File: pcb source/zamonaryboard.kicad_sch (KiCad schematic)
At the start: 17 parts, among them J1 USB_C_Receptacle_USB2.0_14P, SW1 SW_Push, U1 ESP32-S2, U2 ME6211C33M5, Y1 Crystal_GND24

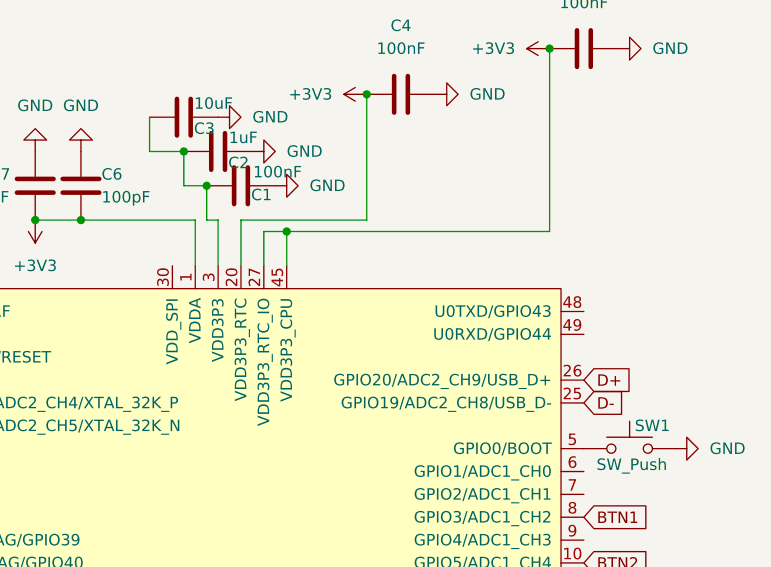
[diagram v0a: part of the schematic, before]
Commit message: Added jlcpcb component annotations, small improvements
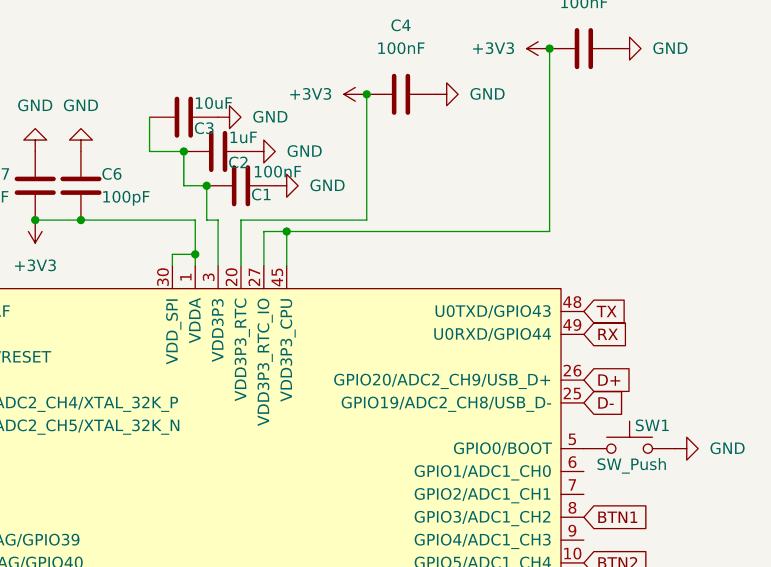
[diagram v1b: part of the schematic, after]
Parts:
- C1, C4, C5: LCSC (none) -> C14663
- C2, C7: LCSC (none) -> C15849
- C3: LCSC (none) -> C19702
- C6: LCSC (none) -> C14665
- C8, C9: LCSC (none) -> C63339
- R1, R2: LCSC (none) -> C23186
- Y1: LCSC (none) -> C9010
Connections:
- net +3V3: now also U1.30 (VDD_SPI)
- net TX: now reaches U1.48 (U0TXD/GPIO43)
- net RX: now reaches U1.49 (U0RXD/GPIO44)
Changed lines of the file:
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@@
 	)
 	(junction
+		(at 134.62 48.26)
+		(diameter 0)
+		(color 0 0 0 0)
+	)
+	(junction
 		(at 39.37 114.3)
 		(diameter 0)
@@
 	(wire
 		(pts
+			(xy 137.16 44.45) (xy 137.16 49.53)
+		)
+		(stroke
+			(width 0)
+			(type default)
+		)
+	)
+	(wire
+		(pts
 			(xy 133.35 36.83) (xy 133.35 40.64)
 		)
@@
 	(wire
 		(pts
-			(xy 137.16 49.53) (xy 137.16 44.45)
+			(xy 50.8 48.26) (xy 53.34 48.26)
 		)
 		(stroke
@@
 	(wire
 		(pts
-			(xy 50.8 48.26) (xy 53.34 48.26)
+			(xy 95.25 74.93) (xy 95.25 77.47)
 		)
 		(stroke
@@
 	(wire
 		(pts
-			(xy 95.25 74.93) (xy 95.25 77.47)
+			(xy 53.34 43.18) (xy 53.34 40.64)
 		)
 		(stroke
@@
 	(wire
 		(pts
-			(xy 53.34 43.18) (xy 53.34 40.64)
+			(xy 95.25 69.85) (xy 95.25 72.39)
 		)
 		(stroke
@@
 	(wire
 		(pts
-			(xy 95.25 69.85) (xy 95.25 72.39)
+			(xy 134.62 48.26) (xy 134.62 44.45)
 		)
 		(stroke
@@
 	(wire
 		(pts
+			(xy 132.08 48.26) (xy 134.62 48.26)
+		)
+		(stroke
+			(width 0)
+			(type default)
+		)
+	)
+	(wire
+		(pts
 			(xy 95.25 72.39) (xy 101.6 72.39)
 		)
@@
 	(wire
 		(pts
-			(xy 134.62 49.53) (xy 134.62 44.45)
+			(xy 134.62 49.53) (xy 134.62 48.26)
 		)
 		(stroke
@@
 	(wire
 		(pts
+			(xy 132.08 48.26) (xy 132.08 49.53)
+		)
+		(stroke
+			(width 0)
+			(type default)
+		)
+	)
+	(wire
+		(pts
 			(xy 153.67 44.45) (xy 153.67 30.48)
 		)
@@
 		)
 	)
+	(global_label "TX"
+		(shape input)
+		(at 177.8 54.61 0)
+		(fields_autoplaced yes)
+		(effects
+			(font
+				(size 1.27 1.27)
+			)
+			(justify left)
+		)
+		(property "Intersheetrefs" "${INTERSHEET_REFS}"
+			(at 182.9623 54.61 0)
+			(effects
+				(font
+					(size 1.27 1.27)
+				)
+				(justify left)
+				(hide yes)
+			)
+		)
+	)
 	(global_label "D+"
 		(shape input)
@@
 		)
 	)
+	(global_label "RX"
+		(shape input)
+		(at 177.8 57.15 0)
+		(fields_autoplaced yes)
+		(effects
+			(font
+				(size 1.27 1.27)
+			)
+			(justify left)
+		)
+		(property "Intersheetrefs" "${INTERSHEET_REFS}"
+			(at 183.2647 57.15 0)
+			(effects
+				(font
+					(size 1.27 1.27)
+				)
+				(justify left)
+				(hide yes)
+			)
+		)
+	)
 	(global_label "D-"
 		(shape input)
@@
 			)
 		)
+		(property "LCSC" "C14665"
+			(at 121.92 40.64 0)
+			(effects
+				(font
+					(size 1.27 1.27)
+				)
+				(hide yes)
+			)
+		)
 		(pin "2"
 		)
@@
 			)
 		)
+		(property "LCSC" "C19702"
+			(at 133.35 33.02 90)
+			(effects
+				(font
+					(size 1.27 1.27)
+				)
+				(hide yes)
+			)
+		)
 		(pin "2"
 		)
@@
 			)
 		)
+		(property "LCSC" "C9010"
+			(at 71.12 73.66 90)
+			(effects
+				(font
+					(size 1.27 1.27)
+				)
+				(hide yes)
+			)
+		)
 		(pin "3"
 		)
@@
 			)
 		)
+		(property "LCSC" "C14663"
+			(at 177.8 25.4 90)
+			(effects
+				(font
+					(size 1.27 1.27)
+				)
+				(hide yes)
+			)
+		)
 		(pin "2"
 		)
@@
 			)
 		)
+		(property "LCSC" "C15849"
+			(at 137.16 36.83 90)
+			(effects
+				(font
+					(size 1.27 1.27)
+				)
+				(hide yes)
+			)
+		)
 		(pin "2"
 		)
@@
 			)
 		)
+		(property "LCSC" "C14663"
+			(at 139.7 40.64 90)
+			(effects
+				(font
+					(size 1.27 1.27)
+				)
+				(hide yes)
+			)
+		)
 		(pin "2"
 		)
@@
 			)
 		)
+		(property "LCSC" "C15849"
+			(at 116.84 40.64 0)
+			(effects
+				(font
+					(size 1.27 1.27)
+				)
+				(hide yes)
+			)
+		)
 		(pin "2"
 		)
@@
 			)
 		)
+		(property "LCSC" "C63339"
+			(at 63.5 83.82 90)
+			(effects
+				(font
+					(size 1.27 1.27)
+				)
+				(hide yes)
+			)
+		)
 		(pin "2"
 		)
@@
 			)
 		)
+		(property "LCSC" "C14663"
+			(at 157.48 30.48 90)
+			(effects
+				(font
+					(size 1.27 1.27)
+				)
+				(hide yes)
+			)
+		)
 		(pin "2"
 		)
@@
 			)
 		)
+		(property "LCSC" "C63339"
+			(at 63.5 63.5 90)
+			(effects
+				(font
+					(size 1.27 1.27)
+				)
+				(hide yes)
+			)
+		)
 		(pin "2"
 		)
@@
 			)
 		)
+		(property "LCSC" "C23186"
+			(at 54.61 33.02 90)
+			(effects
+				(font
+					(size 1.27 1.27)
+				)
+				(hide yes)
+			)
+		)
 		(pin "2"
 		)
@@
 			(effects
 				(font
+					(size 1.27 1.27)
+				)
+				(hide yes)
+			)
+		)
+		(property "LCSC" "C23186"
+			(at 54.61 35.56 90)
+			(effects
+				(font

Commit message: big improvements to pcb
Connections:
- net +3V3: now also C1.1, C2.1, C3.1, U1.3 (VDD3P3), U1.4 (VDD3P3)
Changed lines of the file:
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@@
+	)
+	(junction
+		(at 129.54 33.02)
+		(diameter 0)
+		(color 0 0 0 0)
 	)
 	(junction
@@
 					(unit 1)
 				)
+			)
+		)
+	)
+	(symbol
+		(lib_id "power:+3V3")
+		(at 129.54 33.02 0)
+		(unit 1)
+		(exclude_from_sim no)
+		(in_bom yes)
+		(on_board yes)
+		(dnp no)
+		(property "Reference" "#PWR026"
+			(at 129.54 36.83 0)
+			(effects
+				(font
+					(size 1.27 1.27)
+				)
+				(hide yes)
+			)
+		)
+		(property "Value" "+3V3"
+			(at 128.524 29.718 0)
+			(effects
+				(font
+					(size 1.27 1.27)
+				)
+			)
+		)
+		(property "Footprint" ""
+			(at 129.54 33.02 0)
+			(effects
+				(font
+					(size 1.27 1.27)
+				)
+				(hide yes)
+			)
+		)
+		(property "Datasheet" ""
+			(at 129.54 33.02 0)
+			(effects
+				(font
+					(size 1.27 1.27)
+				)
+				(hide yes)
+			)
+		)
+		(property "Description" "Power symbol creates a global label with name \"+3V3\""
+			(at 129.54 33.02 0)
+			(effects
+				(font
+					(size 1.27 1.27)
+				)
+				(hide yes)
+			)
+		)
+		(pin "1"
+		)
+		(instances
+			(project "zamonaryboard"
+				(path "/d5ea9308-ab10-4197-867c-fba653905f7c"
+					(reference "#PWR026")
+					(unit 1)
+				)

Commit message: exported gerber files for prototype 1.3, cleanup
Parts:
- C8, C9: footprint Capacitor_SMD:C_0805_2012Metric_Pad1.18x1.45mm_HandSolder -> Capacitor_SMD:C_0603_1608Metric_Pad1.08x0.95mm_HandSolder
- Y1: footprint Crystal:Crystal_SMD_3225-4Pin_3.2x2.5mm_HandSoldering -> Crystal:Crystal_SMD_3225-4Pin_3.2x2.5mm
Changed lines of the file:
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@@
 			)
 		)
-		(property "Footprint" "Crystal:Crystal_SMD_3225-4Pin_3.2x2.5mm_HandSoldering"
+		(property "Footprint" "Crystal:Crystal_SMD_3225-4Pin_3.2x2.5mm"
 			(at 71.12 73.66 0)
 			(effects
@@
 			)
 		)
-		(property "Footprint" "Capacitor_SMD:C_0805_2012Metric_Pad1.18x1.45mm_HandSolder"
+		(property "Footprint" "Capacitor_SMD:C_0603_1608Metric_Pad1.08x0.95mm_HandSolder"
 			(at 67.31 82.8548 0)
 			(effects
@@
 			)
 		)
-		(property "Footprint" "Capacitor_SMD:C_0805_2012Metric_Pad1.18x1.45mm_HandSolder"
+		(property "Footprint" "Capacitor_SMD:C_0603_1608Metric_Pad1.08x0.95mm_HandSolder"
 			(at 67.31 62.5348 0)
 			(effects

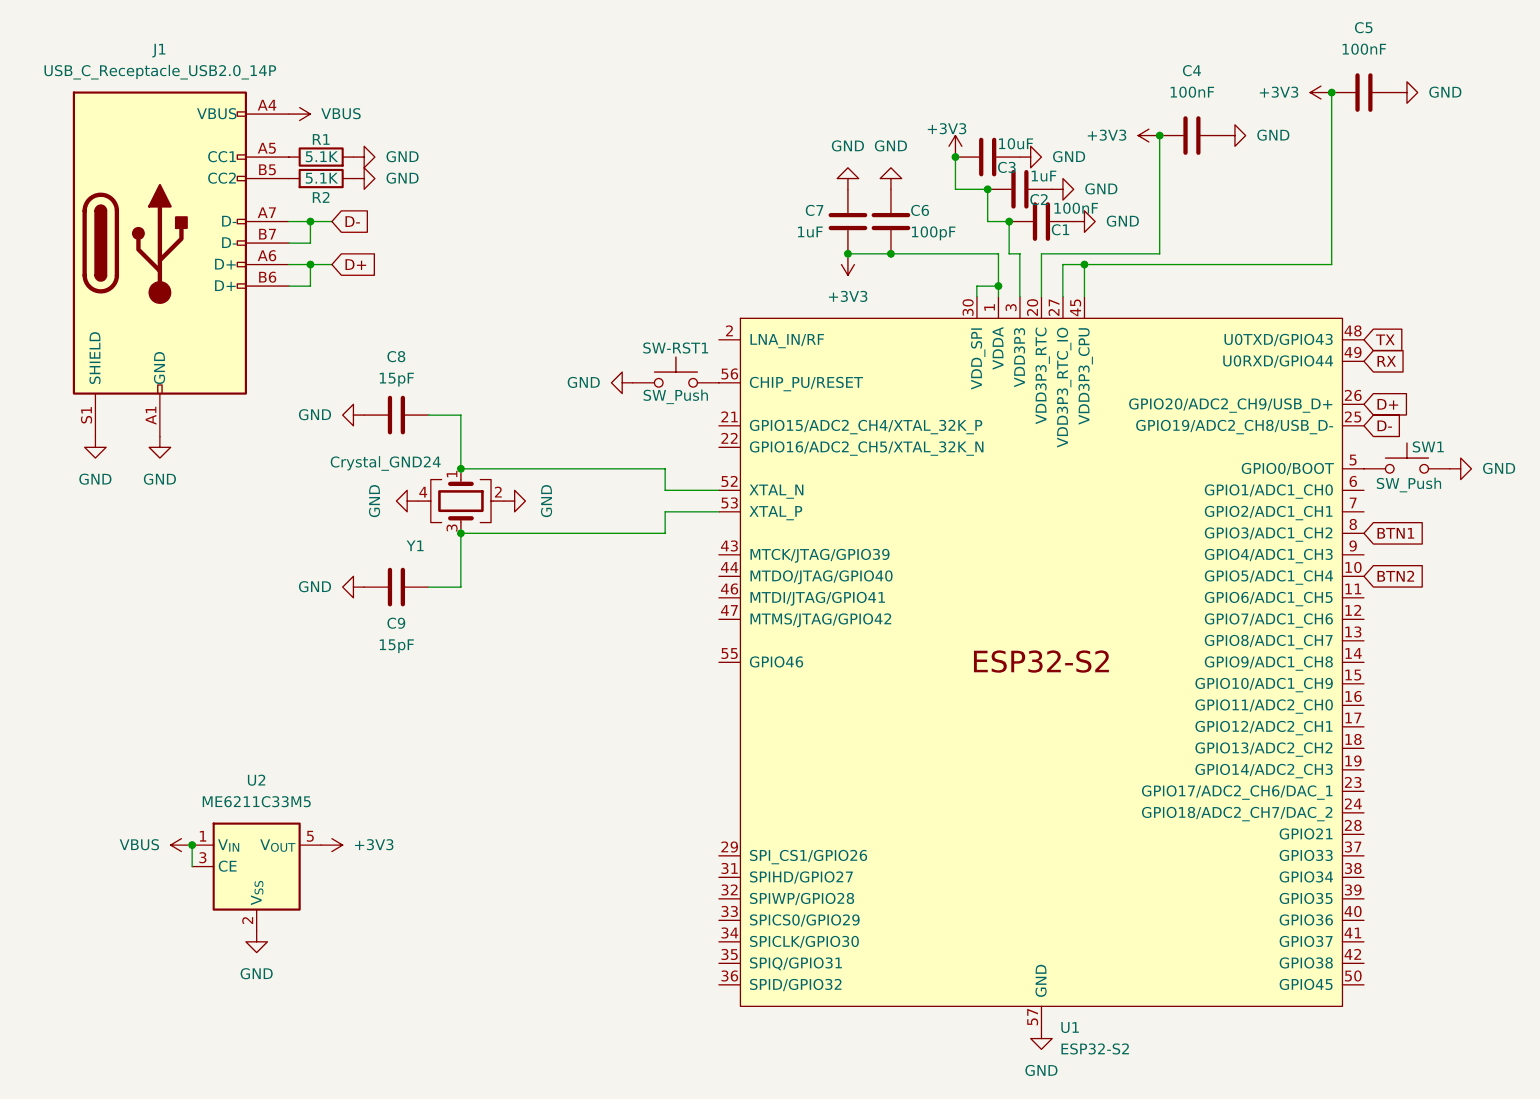
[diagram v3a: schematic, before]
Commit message: Many improvements to pcb and scheme, added testpoints for easier debugging
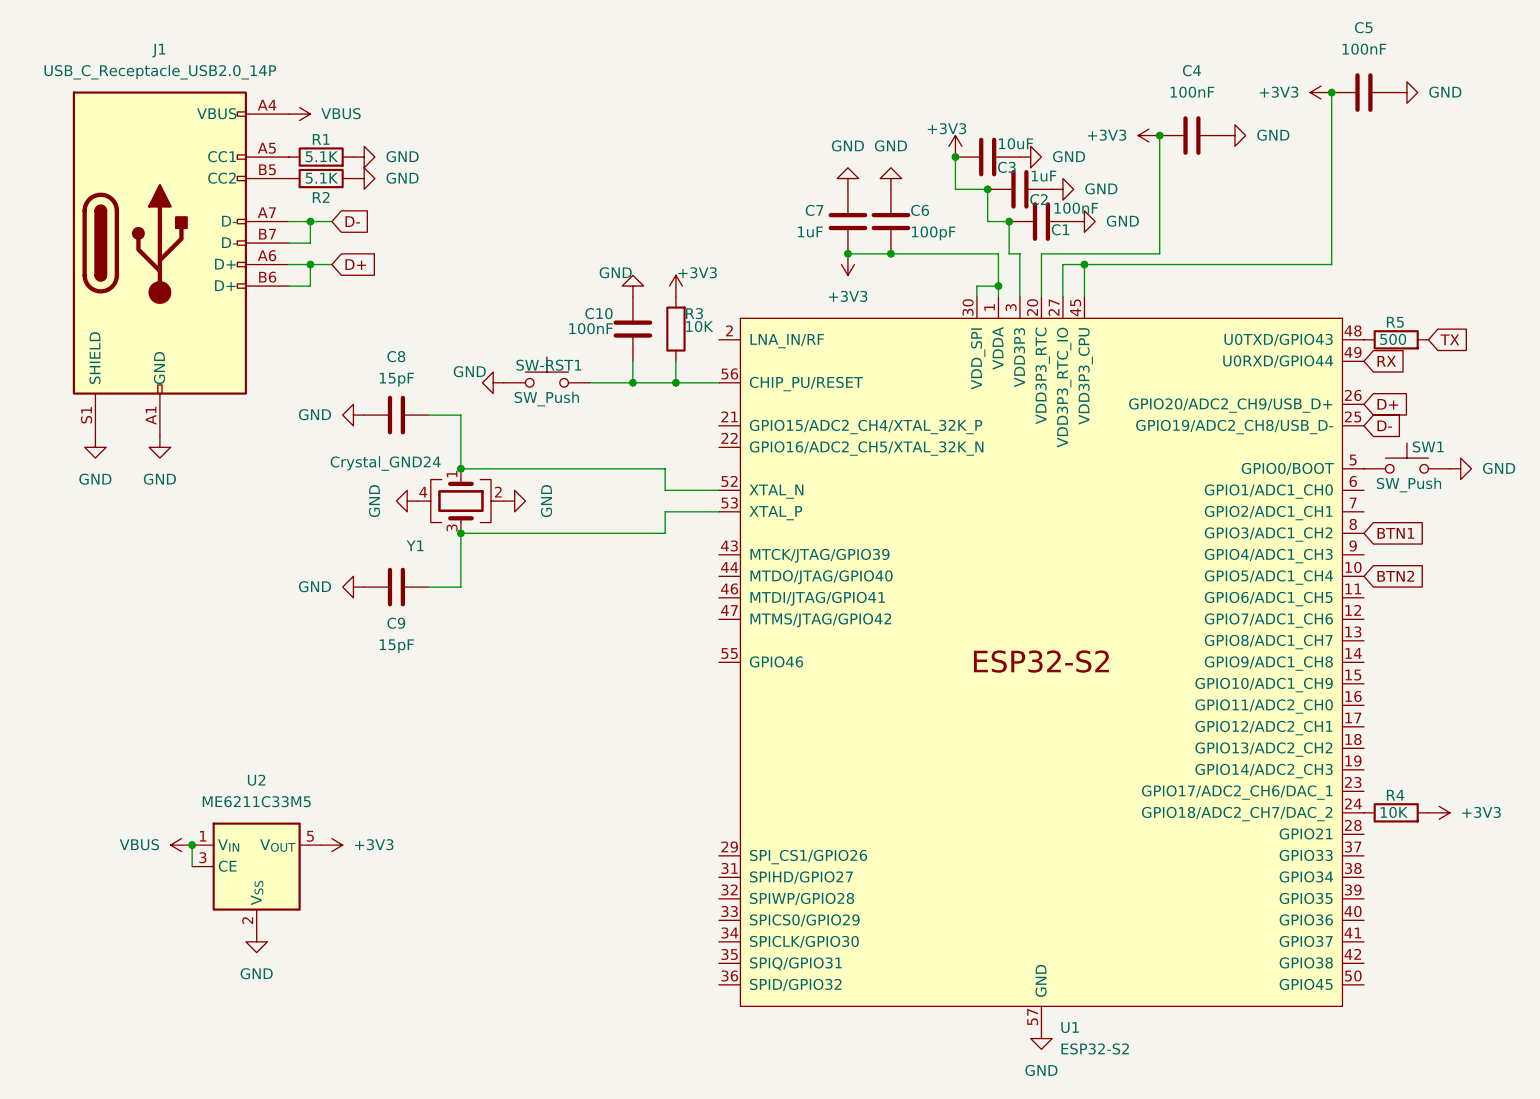
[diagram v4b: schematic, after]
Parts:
- added C10: 100nF, Capacitor_SMD:C_0603_1608Metric, symbol Device:C
- added R3, R4: 10K, Resistor_SMD:R_0603_1608Metric, symbol Device:R
- added R5: 500, Resistor_SMD:R_0603_1608Metric, symbol Device:R
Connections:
- net +3V3: now also R3.2, R4.2
- net GND: now also C10.2
- net TX: now also R5.2; no longer U1.48 (U0TXD/GPIO43)
- net at U1.24 (GPIO18/ADC2_CH7/DAC_2): now also R4.1
- net at SW-RST1.2, U1.56 (CHIP_PU/RESET): now also C10.1, R3.1
- new net: R5.1, U1.48 (U0TXD/GPIO43)
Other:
- moved on the sheet: SW-RST1

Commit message: Improvements on pcb, more components, better routing and better labling.
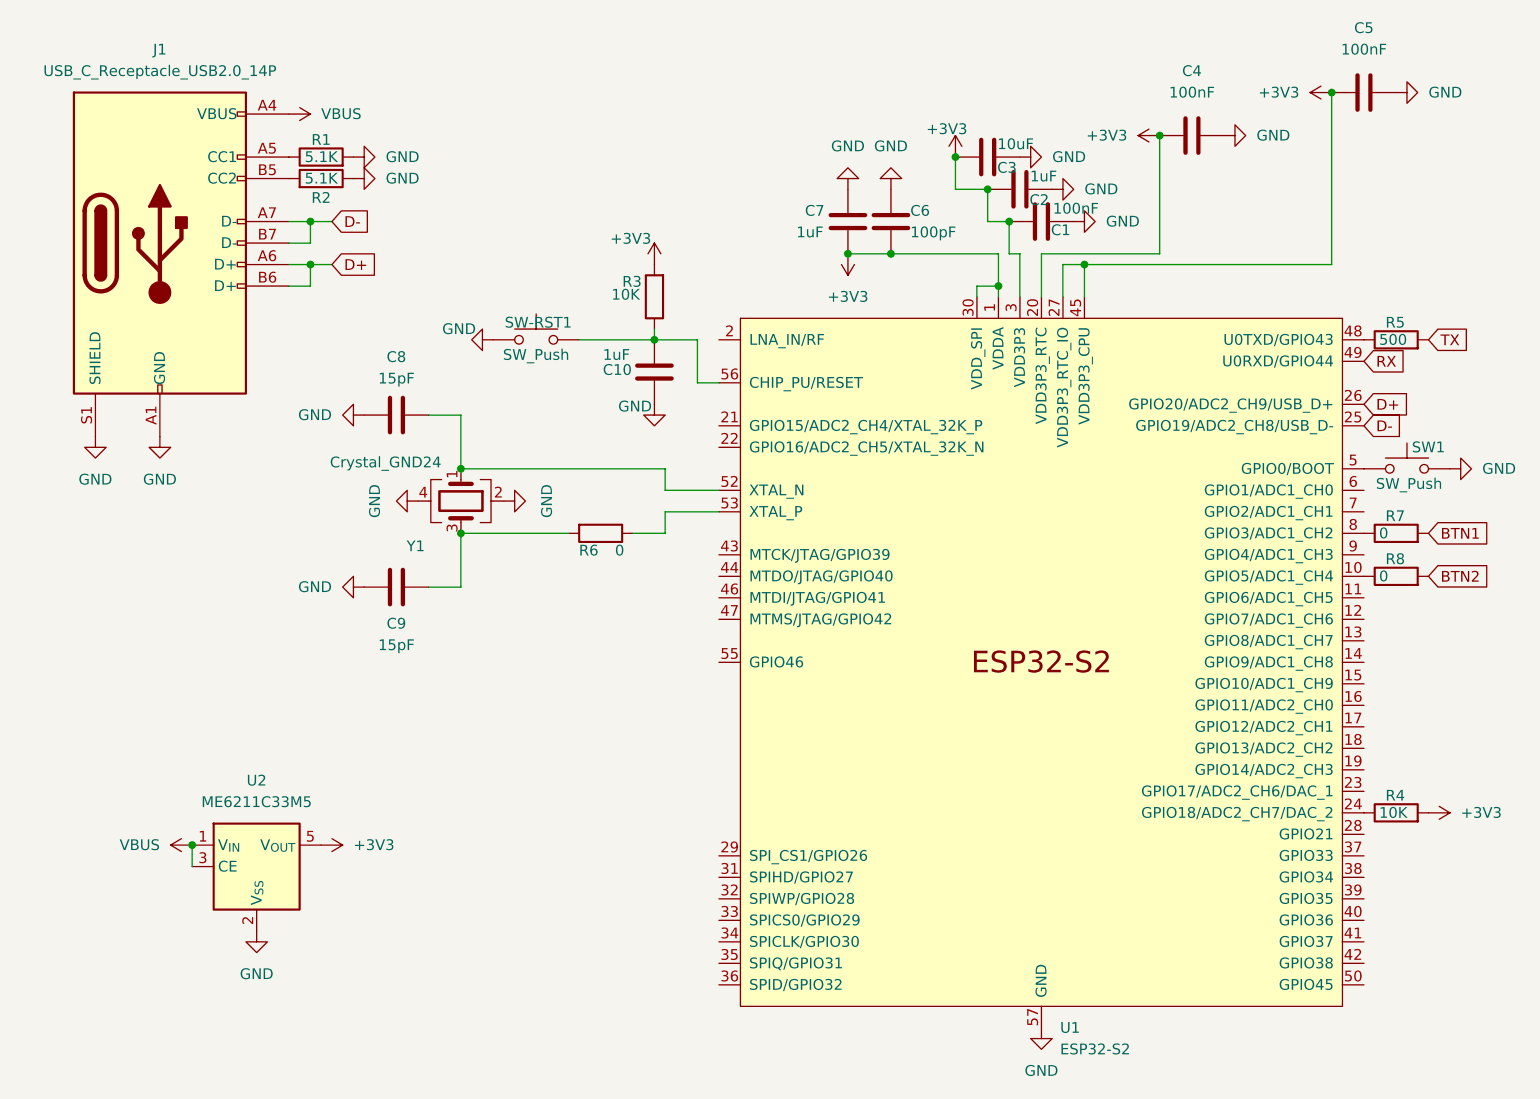
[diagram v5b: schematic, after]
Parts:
- added R6, R7, R8: 0, Resistor_SMD:R_0603_1608Metric, symbol Device:R
- C10: value 100nF -> 1uF
- C8, C9: footprint Capacitor_SMD:C_0603_1608Metric_Pad1.08x0.95mm_HandSolder -> Capacitor_SMD:C_0603_1608Metric
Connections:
- net BTN1: now also R7.2; no longer U1.8 (GPIO3/ADC1_CH2)
- net BTN2: now also R8.2; no longer U1.10 (GPIO5/ADC1_CH4)
- net at C9.2, Y1.3: now also R6.2; no longer U1.53 (XTAL_P)
- new net: R7.1, U1.8 (GPIO3/ADC1_CH2)
- new net: R8.1, U1.10 (GPIO5/ADC1_CH4)
- new net: R6.1, U1.53 (XTAL_P)
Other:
- moved on the sheet: C10, R3, SW-RST1
